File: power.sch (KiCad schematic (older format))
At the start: 13 parts, among them J9 POWER, U7 LM1117-3.3, U8 LM1117-5.0

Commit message: work on schematic
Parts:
- removed C3: 10u, Capacitors_SMD:CP_Elec_6.3x4.5, symbol CP1
- removed C4, C5, C6, C7: 22u, symbol CP1
- removed C8, C9: 100n, symbol C
- removed U7: LM1117-3.3, TO_SOT_Packages_SMD:SOT-223, symbol LM1117-3.3
- removed U8: LM1117-5.0, symbol LM1117-5.0
- added C201, C206, C211: 100n, Capacitors_SMD:C_0603, symbol CP1
- added C202, C207, C212: 22u, Capacitors_SMD:CP_Elec_5x5.8, symbol CP1
- added C203, C208, C209, C210, C213: 100n, Capacitors_SMD:C_0603, symbol C
- added C205: 47u, Capacitors_SMD:CP_Elec_6.3x5.7, symbol CP1
- added D202: LM4040CIM3-10.0, TO_SOT_Packages_SMD:SOT-23, symbol D_Schottky_ALT
- added D203: LM4040AIM3-2.0, TO_SOT_Packages_SMD:SOT-23, symbol D_Schottky_ALT
- added L201, L202, L203: Bead, Resistors_SMD:R_0603, symbol Ferrite_Bead
- added R201, R202: 1k, Resistors_SMD:R_0603, symbol R
- added R203: 10k, Resistors_SMD:R_0603, symbol R
- added U201, U202: LM1117-3.3, TO_SOT_Packages_SMD:SOT-223-3Lead_TabPin2, symbol LM1117-3.3
- added U203: LM1117-5.0, TO_SOT_Packages_SMD:SOT-223-3Lead_TabPin2, symbol LM1117-5.0
- added U204: STMPS2151, TO_SOT_Packages_SMD:SOT-23-5, symbol STMPS2141
- 1N5819HW201: renamed from D4; value D -> D204
- C204: renamed from C2; value 10u -> 47u; footprint Capacitors_SMD:CP_Elec_6.3x4.5 -> Capacitors_SMD:CP_Elec_6.3x5.7; MFN (none) -> Panasonic; MFP (none) -> EEE-FK1V470P
- D201: renamed from D3; value D -> 1N5819HW
- renumbered J9 to J201
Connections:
- net +12V: now also L201.2, L202.2, L203.2
- net +3.3VA: now also C207.1, C208.1, R202.1, U202.2 (VO)
- net +3V3: now also C202.1, C203.1, U201.2 (VO)
- net +5V: now also C212.1, C213.1, U203.2 (VO), U204.5 (IN)
- net -12V: now also C205.2, R201.1
- net GND: now also C201.2, C202.2, C203.2, C205.1, C206.2, C207.2, C208.2, C209.2, C210.2, C211.2, C212.2, C213.2, D202.1 (K), D203.2 (A), R203.2, U201.1 (GND), U202.1 (GND), U203.1 (GND), U204.2 (GND)
- net at J201.1 (Pin_1), J201.2 (Pin_2): now also 1N5819HW201.1 (K); no longer D201.2 (A)
- net at J201.10 (Pin_10), J201.9 (Pin_9): now also D201.2 (A); no longer 1N5819HW201.1 (K)
- new net: C201.1, L201.1, U201.3 (VI)
- new net: C206.1, L202.1, U202.3 (VI)
- new net: C211.1, L203.1, U203.3 (VI)
- new net AREF_-10V: C209.1, D202.2 (A), R201.2
- new net AREF_2.048V: C210.1, D203.1 (K), R202.2
- new net USB_5V: U204.1 (OUT)
- new net USB_PWR_EN: R203.1, U204.4 (EN)
- new net USB_PWR_FAULT: U204.3 (~FAULT)

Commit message: work in progress
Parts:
- C201, C203, C206, C208, C209, C210, C211, C213: MFN (none) -> Murata; MFP (none) -> GRM188R71E104JA01J
- D201: MFN (none) -> Diodes Inc.; MFP (none) -> 1N5819HW-7-F
- D204: renamed from 1N5819HW201; value D204 -> 1N5819HW; MFN (none) -> Diodes Inc.; MFP (none) -> 1N5819HW-7-F
- R201, R202: MFN (none) -> Panasonic; MFP (none) -> ERJ-3EKF1001V
- R203: MFN (none) -> Panasonic; MFP (none) -> ERJ-3EKF1002V

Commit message: work in progress
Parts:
- removed C201, C206, C211: 100n, Capacitors_SMD:C_0603, symbol CP1
- added C201, C206, C211: 100n, Capacitors_SMD:C_0603, symbol C
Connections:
- net GND: now also C201.2, C206.2, C211.2
- net at L201.1, U201.3 (VI): now also C201.1
- net at L202.1, U202.3 (VI): now also C206.1
- net at L203.1, U203.3 (VI): now also C211.1
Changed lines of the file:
@@
 $EndDescr
 $Comp
-L +12V #PWR022
+L +12V #PWR023
 U 1 1 59ADCE23
 P 1400 2500
-F 0 "#PWR022" H 1400 2350 50  0001 C CNN
+F 0 "#PWR023" H 1400 2350 50  0001 C CNN
 F 1 "+12V" H 1400 2640 50  0000 C CNN
 F 2 "" H 1400 2500 50  0001 C CNN
@@
 $EndComp
 $Comp
-L GND #PWR023
+L GND #PWR024
 U 1 1 59ADD2AE
 P 2800 2900
-F 0 "#PWR023" H 2800 2650 50  0001 C CNN
+F 0 "#PWR024" H 2800 2650 50  0001 C CNN
 F 1 "GND" H 2800 2750 50  0000 C CNN
 F 2 "" H 2800 2900 50  0001 C CNN
@@
 $EndComp
 $Comp
-L +12V #PWR024
+L +12V #PWR025
 U 1 1 59ADD597
 P 3800 2300
-F 0 "#PWR024" H 3800 2150 50  0001 C CNN
+F 0 "#PWR025" H 3800 2150 50  0001 C CNN
 F 1 "+12V" H 3800 2440 50  0000 C CNN
 F 2 "" H 3800 2300 50  0001 C CNN
@@
 $EndComp
 $Comp
-L GND #PWR025
+L GND #PWR026
 U 1 1 59ADD670
 P 3600 2900
-F 0 "#PWR025" H 3600 2650 50  0001 C CNN
+F 0 "#PWR026" H 3600 2650 50  0001 C CNN
 F 1 "GND" H 3600 2750 50  0000 C CNN
 F 2 "" H 3600 2900 50  0001 C CNN
@@
 $EndComp
 $Comp
-L CP1 C201
-U 1 1 59DEC568
-P 5300 1950
-F 0 "C201" H 5325 2050 50  0000 L CNN
-F 1 "100n" H 5325 1850 50  0000 L CNN
-F 2 "Capacitors_SMD:C_0603" H 5300 1950 50  0001 C CNN
-F 3 "http://datasheet.octopart.com/GRM188R71E104JA01J-Murata-datasheet-66077098.pdf" H 5300 1950 50  0001 C CNN
-F 4 "Murata" H 5325 2150 50  0001 C CNN "MFN"
-F 5 "GRM188R71E104JA01J" H 5325 2150 50  0001 C CNN "MFP"
-	1    5300 1950
-	1    0    0    -1
-$EndComp
-$Comp
 L CP1 C202
 U 1 1 59DEC56E
@@
 $EndComp
 $Comp
-L GND #PWR026
+L GND #PWR027
 U 1 1 59DEC57A
 P 5300 2200
-F 0 "#PWR026" H 5300 1950 50  0001 C CNN
+F 0 "#PWR027" H 5300 1950 50  0001 C CNN
 F 1 "GND" H 5300 2050 50  0000 C CNN
 F 2 "" H 5300 2200 50  0001 C CNN
@@
 $EndComp
 $Comp
-L GND #PWR027
+L GND #PWR028
 U 1 1 59DEC580
 P 6300 2200
-F 0 "#PWR027" H 6300 1950 50  0001 C CNN
+F 0 "#PWR028" H 6300 1950 50  0001 C CNN
 F 1 "GND" H 6300 2050 50  0000 C CNN
 F 2 "" H 6300 2200 50  0001 C CNN
@@
 $EndComp
 $Comp
-L GND #PWR028
+L GND #PWR029
 U 1 1 59DEC586
 P 6600 2200
-F 0 "#PWR028" H 6600 1950 50  0001 C CNN
+F 0 "#PWR029" H 6600 1950 50  0001 C CNN
 F 1 "GND" H 6600 2050 50  0000 C CNN
 F 2 "" H 6600 2200 50  0001 C CNN
@@
 $EndComp
 $Comp
-L +3V3 #PWR029
+L +3V3 #PWR030
 U 1 1 59DEC592
 P 6600 1600
-F 0 "#PWR029" H 6600 1450 50  0001 C CNN
+F 0 "#PWR030" H 6600 1450 50  0001 C CNN
 F 1 "+3V3" H 6600 1740 50  0000 C CNN
 F 2 "" H 6600 1600 50  0001 C CNN
@@
 $EndComp
 $Comp
-L GND #PWR030
+L GND #PWR031
 U 1 1 59DEC598
 P 5800 2200
-F 0 "#PWR030" H 5800 1950 50  0001 C CNN
+F 0 "#PWR031" H 5800 1950 50  0001 C CNN
 F 1 "GND" H 5800 2050 50  0000 C CNN
 F 2 "" H 5800 2200 50  0001 C CNN
@@
 $EndComp
 $Comp
-L CP1 C206
-U 1 1 59DEC800
-P 5300 3050
-F 0 "C206" H 5325 3150 50  0000 L CNN
-F 1 "100n" H 5325 2950 50  0000 L CNN
-F 2 "Capacitors_SMD:C_0603" H 5300 3050 50  0001 C CNN
-F 3 "http://datasheet.octopart.com/GRM188R71E104JA01J-Murata-datasheet-66077098.pdf" H 5300 3050 50  0001 C CNN
-F 4 "Murata" H 5325 3250 50  0001 C CNN "MFN"
-F 5 "GRM188R71E104JA01J" H 5325 3250 50  0001 C CNN "MFP"
-	1    5300 3050
-	1    0    0    -1
-$EndComp
-$Comp
 L C C208
 U 1 1 59DEC80C
@@
 $EndComp
 $Comp
-L GND #PWR031
+L GND #PWR032
 U 1 1 59DEC812
 P 5300 3300
-F 0 "#PWR031" H 5300 3050 50  0001 C CNN
+F 0 "#PWR032" H 5300 3050 50  0001 C CNN
 F 1 "GND" H 5300 3150 50  0000 C CNN
 F 2 "" H 5300 3300 50  0001 C CNN
@@
 $EndComp
 $Comp
-L GND #PWR032
+L GND #PWR033
 U 1 1 59DEC818
 P 6300 3300
-F 0 "#PWR032" H 6300 3050 50  0001 C CNN
+F 0 "#PWR033" H 6300 3050 50  0001 C CNN
 F 1 "GND" H 6300 3150 50  0000 C CNN
 F 2 "" H 6300 3300 50  0001 C CNN
@@
 $EndComp
 $Comp
-L GND #PWR033
+L GND #PWR034
 U 1 1 59DEC81E
 P 6600 3300
-F 0 "#PWR033" H 6600 3050 50  0001 C CNN
+F 0 "#PWR034" H 6600 3050 50  0001 C CNN
 F 1 "GND" H 6600 3150 50  0000 C CNN
 F 2 "" H 6600 3300 50  0001 C CNN
@@
 $EndComp
 $Comp
-L GND #PWR034
+L GND #PWR035
 U 1 1 59DEC82A
 P 5800 3300
-F 0 "#PWR034" H 5800 3050 50  0001 C CNN
+F 0 "#PWR035" H 5800 3050 50  0001 C CNN
 F 1 "GND" H 5800 3150 50  0000 C CNN
 F 2 "" H 5800 3300 50  0001 C CNN
@@
 $EndComp
 $Comp
-L +12V #PWR035
+L +12V #PWR036
 U 1 1 59DECCAB
 P 4800 1600
-F 0 "#PWR035" H 4800 1450 50  0001 C CNN
+F 0 "#PWR036" H 4800 1450 50  0001 C CNN
 F 1 "+12V" H 4800 1740 50  0000 C CNN
 F 2 "" H 4800 1600 50  0001 C CNN
@@
 $EndComp
 $Comp
-L +3.3VA #PWR036
+L +3.3VA #PWR037
 U 1 1 59DED3E1
 P 6600 2700
-F 0 "#PWR036" H 6600 2550 50  0001 C CNN
+F 0 "#PWR037" H 6600 2550 50  0001 C CNN
 F 1 "+3.3VA" H 6600 2840 50  0000 C CNN
 F 2 "" H 6600 2700 50  0001 C CNN
@@
 $EndComp
 $Comp
-L CP1 C211
-U 1 1 59DED9B9
-P 5300 4150
-F 0 "C211" H 5325 4250 50  0000 L CNN
-F 1 "100n" H 5325 4050 50  0000 L CNN
-F 2 "Capacitors_SMD:C_0603" H 5300 4150 50  0001 C CNN
-F 3 "http://datasheet.octopart.com/GRM188R71E104JA01J-Murata-datasheet-66077098.pdf" H 5300 4150 50  0001 C CNN
-F 4 "Murata" H 5325 4350 50  0001 C CNN "MFN"
-F 5 "GRM188R71E104JA01J" H 5325 4350 50  0001 C CNN "MFP"
-	1    5300 4150
-	1    0    0    -1
-$EndComp
-$Comp
 L C C213
 U 1 1 59DED9C5
@@
 $EndComp
 $Comp
-L GND #PWR037
+L GND #PWR038
 U 1 1 59DED9CB
 P 5300 4400
-F 0 "#PWR037" H 5300 4150 50  0001 C CNN
+F 0 "#PWR038" H 5300 4150 50  0001 C CNN
 F 1 "GND" H 5300 4250 50  0000 C CNN
 F 2 "" H 5300 4400 50  0001 C CNN
@@
 $EndComp
 $Comp
-L GND #PWR038
+L GND #PWR039
 U 1 1 59DED9D1
 P 6300 4400
-F 0 "#PWR038" H 6300 4150 50  0001 C CNN
+F 0 "#PWR039" H 6300 4150 50  0001 C CNN
 F 1 "GND" H 6300 4250 50  0000 C CNN
 F 2 "" H 6300 4400 50  0001 C CNN
@@
 $EndComp
 $Comp
-L GND #PWR039
+L GND #PWR040
 U 1 1 59DED9D7
 P 6600 4400
-F 0 "#PWR039" H 6600 4150 50  0001 C CNN
+F 0 "#PWR040" H 6600 4150 50  0001 C CNN
 F 1 "GND" H 6600 4250 50  0000 C CNN
 F 2 "" H 6600 4400 50  0001 C CNN
@@
 $EndComp
 $Comp
-L GND #PWR040
+L GND #PWR041
 U 1 1 59DED9DD
 P 5800 4400
-F 0 "#PWR040" H 5800 4150 50  0001 C CNN
+F 0 "#PWR041" H 5800 4150 50  0001 C CNN
 F 1 "GND" H 5800 4250 50  0000 C CNN
 F 2 "" H 5800 4400 50  0001 C CNN
@@
 $EndComp
 $Comp
-L +5V #PWR041
+L +5V #PWR042
 U 1 1 59DEDB3A
 P 6600 3800
-F 0 "#PWR041" H 6600 3650 50  0001 C CNN
+F 0 "#PWR042" H 6600 3650 50  0001 C CNN
 F 1 "+5V" H 6600 3940 50  0000 C CNN
 F 2 "" H 6600 3800 50  0001 C CNN
@@
 $EndComp
 $Comp
-L GND #PWR042
+L GND #PWR043
 U 1 1 59DF1FC9
 P 7900 3400
-F 0 "#PWR042" H 7900 3150 50  0001 C CNN
+F 0 "#PWR043" H 7900 3150 50  0001 C CNN
 F 1 "GND" H 7900 3250 50  0000 C CNN
 F 2 "" H 7900 3400 50  0001 C CNN
@@
 $EndComp
 $Comp
-L +5V #PWR043
+L +5V #PWR044
 U 1 1 59DFDC6E
 P 8400 4000
-F 0 "#PWR043" H 8400 3850 50  0001 C CNN
+F 0 "#PWR044" H 8400 3850 50  0001 C CNN
 F 1 "+5V" H 8400 4140 50  0000 C CNN
 F 2 "" H 8400 4000 50  0001 C CNN
@@
 $EndComp
 $Comp
-L GND #PWR044
+L GND #PWR045
 U 1 1 59DFDCE5
 P 8400 4700
-F 0 "#PWR044" H 8400 4450 50  0001 C CNN
+F 0 "#PWR045" H 8400 4450 50  0001 C CNN
 F 1 "GND" H 8400 4550 50  0000 C CNN
 F 2 "" H 8400 4700 50  0001 C CNN
@@
 $EndComp
 $Comp
-L GND #PWR045
+L GND #PWR046
 U 1 1 59E00E5E
 P 8200 4700
-F 0 "#PWR045" H 8200 4450 50  0001 C CNN
+F 0 "#PWR046" H 8200 4450 50  0001 C CNN
 F 1 "GND" H 8200 4550 50  0000 C CNN
 F 2 "" H 8200 4700 50  0001 C CNN
@@
 $EndComp
 $Comp
-L GND #PWR046
+L GND #PWR047
 U 1 1 59E08D7D
 P 9400 3400
-F 0 "#PWR046" H 9400 3150 50  0001 C CNN
+F 0 "#PWR047" H 9400 3150 50  0001 C CNN
 F 1 "GND" H 9400 3250 50  0000 C CNN
 F 2 "" H 9400 3400 50  0001 C CNN
@@
 $EndComp
 $Comp
-L +3.3VA #PWR047
+L +3.3VA #PWR048
 U 1 1 59E0BF07
 P 9400 2300
-F 0 "#PWR047" H 9400 2150 50  0001 C CNN
+F 0 "#PWR048" H 9400 2150 50  0001 C CNN
 F 1 "+3.3VA" H 9400 2440 50  0000 C CNN
 F 2 "" H 9400 2300 50  0001 C CNN
@@
 Connection ~ 7900 2800
 Connection ~ 9400 2800
+$Comp
+L C C201
+U 1 1 59E52EDD
+P 5300 1950
+F 0 "C201" H 5325 2050 50  0000 L CNN
+F 1 "100n" H 5325 1850 50  0000 L CNN
+F 2 "Capacitors_SMD:C_0603" H 5338 1800 50  0001 C CNN
+F 3 "http://datasheet.octopart.com/GRM188R71E104JA01J-Murata-datasheet-66077098.pdf" H 5300 1950 50  0001 C CNN
+F 4 "Murata" H 5300 1950 60  0001 C CNN "MFN"
+F 5 "GRM188R71E104JA01J" H 5300 1950 60  0001 C CNN "MFP"
+	1    5300 1950
+	1    0    0    -1
+$EndComp
+$Comp
+L C C206
+U 1 1 59E53513
+P 5300 3050
+F 0 "C206" H 5325 3150 50  0000 L CNN
+F 1 "100n" H 5325 2950 50  0000 L CNN
+F 2 "Capacitors_SMD:C_0603" H 5338 2900 50  0001 C CNN
+F 3 "http://datasheet.octopart.com/GRM188R71E104JA01J-Murata-datasheet-66077098.pdf" H 5300 3050 50  0001 C CNN
+F 4 "Murata" H 5300 3050 60  0001 C CNN "MFN"
+F 5 "GRM188R71E104JA01J" H 5300 3050 60  0001 C CNN "MFP"
+	1    5300 3050
+	1    0    0    -1
+$EndComp
+$Comp
+L C C211
+U 1 1 59E535E8
+P 5300 4150
+F 0 "C211" H 5325 4250 50  0000 L CNN
+F 1 "100n" H 5325 4050 50  0000 L CNN
+F 2 "Capacitors_SMD:C_0603" H 5338 4000 50  0001 C CNN
+F 3 "http://datasheet.octopart.com/GRM188R71E104JA01J-Murata-datasheet-66077098.pdf" H 5300 4150 50  0001 C CNN
+F 4 "Murata" H 5300 4150 60  0001 C CNN "MFN"
+F 5 "GRM188R71E104JA01J" H 5300 4150 60  0001 C CNN "MFP"
+	1    5300 4150
+	1    0    0    -1
+$EndComp
 $EndSCHEMATC

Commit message: redesign in progress
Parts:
- removed C210: 100n, Capacitors_SMD:C_0603, symbol C
- removed D203: LM4040AIM3-2.0, TO_SOT_Packages_SMD:SOT-23, symbol D_Schottky_ALT
- removed R202: 1k, Resistors_SMD:R_0603, symbol R

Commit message: only ground plane left
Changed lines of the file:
@@
 $EndDescr
 $Comp
-L +12V #PWR210
+L +12V #PWR023
 U 1 1 59ADCE23
 P 1400 2500
-F 0 "#PWR210" H 1400 2350 50  0001 C CNN
+F 0 "#PWR023" H 1400 2350 50  0001 C CNN
 F 1 "+12V" H 1400 2640 50  0000 C CNN
 F 2 "" H 1400 2500 50  0001 C CNN
@@
 $EndComp
 $Comp
-L -12V #PWR214
+L -12V #PWR213
 U 1 1 59ADCE37
 P 1400 3100
-F 0 "#PWR214" H 1400 3200 50  0001 C CNN
+F 0 "#PWR213" H 1400 3200 50  0001 C CNN
 F 1 "-12V" H 1400 3250 50  0000 C CNN
 F 2 "" H 1400 3100 50  0001 C CNN
@@
 $EndComp
 $Comp
-L GND #PWR212
+L GND #PWR024
 U 1 1 59ADD2AE
 P 2800 2900
-F 0 "#PWR212" H 2800 2650 50  0001 C CNN
+F 0 "#PWR024" H 2800 2650 50  0001 C CNN
 F 1 "GND" H 2800 2750 50  0000 C CNN
 F 2 "" H 2800 2900 50  0001 C CNN
@@
 $EndComp
 $Comp
-L -12V #PWR215
+L -12V #PWR214
 U 1 1 59ADD571
 P 3800 3300
-F 0 "#PWR215" H 3800 3400 50  0001 C CNN
+F 0 "#PWR214" H 3800 3400 50  0001 C CNN
 F 1 "-12V" H 3800 3450 50  0000 C CNN
 F 2 "" H 3800 3300 50  0001 C CNN
@@
 $EndComp
 $Comp
-L +12V #PWR207
+L +12V #PWR025
 U 1 1 59ADD597
 P 3800 2300
-F 0 "#PWR207" H 3800 2150 50  0001 C CNN
+F 0 "#PWR025" H 3800 2150 50  0001 C CNN
 F 1 "+12V" H 3800 2440 50  0000 C CNN
 F 2 "" H 3800 2300 50  0001 C CNN
@@
 $EndComp
 $Comp
-L GND #PWR213
+L GND #PWR026
 U 1 1 59ADD670
 P 3600 2900
-F 0 "#PWR213" H 3600 2650 50  0001 C CNN
+F 0 "#PWR026" H 3600 2650 50  0001 C CNN
 F 1 "GND" H 3600 2750 50  0000 C CNN
 F 2 "" H 3600 2900 50  0001 C CNN
@@
 $EndComp
 $Comp
-L GND #PWR203
+L GND #PWR027
 U 1 1 59DEC57A
 P 5300 2200
-F 0 "#PWR203" H 5300 1950 50  0001 C CNN
+F 0 "#PWR027" H 5300 1950 50  0001 C CNN
 F 1 "GND" H 5300 2050 50  0000 C CNN
 F 2 "" H 5300 2200 50  0001 C CNN
@@
 $EndComp
 $Comp
-L GND #PWR205
+L GND #PWR028
 U 1 1 59DEC580
 P 6300 2200
-F 0 "#PWR205" H 6300 1950 50  0001 C CNN
+F 0 "#PWR028" H 6300 1950 50  0001 C CNN
 F 1 "GND" H 6300 2050 50  0000 C CNN
 F 2 "" H 6300 2200 50  0001 C CNN
@@
 $EndComp
 $Comp
-L GND #PWR206
+L GND #PWR029
 U 1 1 59DEC586
 P 6600 2200
-F 0 "#PWR206" H 6600 1950 50  0001 C CNN
+F 0 "#PWR029" H 6600 1950 50  0001 C CNN
 F 1 "GND" H 6600 2050 50  0000 C CNN
 F 2 "" H 6600 2200 50  0001 C CNN
@@
 $EndComp
 $Comp
-L +3V3 #PWR202
+L +3V3 #PWR030
 U 1 1 59DEC592
 P 6600 1600
-F 0 "#PWR202" H 6600 1450 50  0001 C CNN
+F 0 "#PWR030" H 6600 1450 50  0001 C CNN
 F 1 "+3V3" H 6600 1740 50  0000 C CNN
 F 2 "" H 6600 1600 50  0001 C CNN
@@
 $EndComp
 $Comp
-L GND #PWR204
+L GND #PWR031
 U 1 1 59DEC598
 P 5800 2200
-F 0 "#PWR204" H 5800 1950 50  0001 C CNN
+F 0 "#PWR031" H 5800 1950 50  0001 C CNN
 F 1 "GND" H 5800 2050 50  0000 C CNN
 F 2 "" H 5800 2200 50  0001 C CNN
@@
 $EndComp
 $Comp
-L GND #PWR216
+L GND #PWR032
 U 1 1 59DEC812
 P 5300 3300
-F 0 "#PWR216" H 5300 3050 50  0001 C CNN
+F 0 "#PWR032" H 5300 3050 50  0001 C CNN
 F 1 "GND" H 5300 3150 50  0000 C CNN
 F 2 "" H 5300 3300 50  0001 C CNN
@@
 $EndComp
 $Comp
-L GND #PWR218
+L GND #PWR033
 U 1 1 59DEC818
 P 6300 3300
-F 0 "#PWR218" H 6300 3050 50  0001 C CNN
+F 0 "#PWR033" H 6300 3050 50  0001 C CNN
 F 1 "GND" H 6300 3150 50  0000 C CNN
 F 2 "" H 6300 3300 50  0001 C CNN
@@
 $EndComp
 $Comp
-L GND #PWR219
+L GND #PWR034
 U 1 1 59DEC81E
 P 6600 3300
-F 0 "#PWR219" H 6600 3050 50  0001 C CNN
+F 0 "#PWR034" H 6600 3050 50  0001 C CNN
 F 1 "GND" H 6600 3150 50  0000 C CNN
 F 2 "" H 6600 3300 50  0001 C CNN
@@
 $EndComp
 $Comp
-L GND #PWR217
+L GND #PWR035
 U 1 1 59DEC82A
 P 5800 3300
-F 0 "#PWR217" H 5800 3050 50  0001 C CNN
+F 0 "#PWR035" H 5800 3050 50  0001 C CNN
 F 1 "GND" H 5800 3150 50  0000 C CNN
 F 2 "" H 5800 3300 50  0001 C CNN
@@
 $EndComp
 $Comp
-L +12V #PWR201
+L +12V #PWR036
 U 1 1 59DECCAB
 P 4800 1600
-F 0 "#PWR201" H 4800 1450 50  0001 C CNN
+F 0 "#PWR036" H 4800 1450 50  0001 C CNN
 F 1 "+12V" H 4800 1740 50  0000 C CNN
 F 2 "" H 4800 1600 50  0001 C CNN
@@
 $EndComp
 $Comp
-L +3.3VA #PWR211
+L +3.3VA #PWR037
 U 1 1 59DED3E1
 P 6600 2700
-F 0 "#PWR211" H 6600 2550 50  0001 C CNN
+F 0 "#PWR037" H 6600 2550 50  0001 C CNN
 F 1 "+3.3VA" H 6600 2840 50  0000 C CNN
 F 2 "" H 6600 2700 50  0001 C CNN
@@
 $EndComp
 $Comp
-L GND #PWR224
+L GND #PWR038
 U 1 1 59DED9CB
 P 5300 4400
-F 0 "#PWR224" H 5300 4150 50  0001 C CNN
+F 0 "#PWR038" H 5300 4150 50  0001 C CNN
 F 1 "GND" H 5300 4250 50  0000 C CNN
 F 2 "" H 5300 4400 50  0001 C CNN
@@
 $EndComp
 $Comp
-L GND #PWR226
+L GND #PWR039
 U 1 1 59DED9D1
 P 6300 4400
-F 0 "#PWR226" H 6300 4150 50  0001 C CNN
+F 0 "#PWR039" H 6300 4150 50  0001 C CNN
 F 1 "GND" H 6300 4250 50  0000 C CNN
 F 2 "" H 6300 4400 50  0001 C CNN
@@
 $EndComp
 $Comp
-L GND #PWR227
+L GND #PWR040
 U 1 1 59DED9D7
 P 6600 4400
-F 0 "#PWR227" H 6600 4150 50  0001 C CNN
+F 0 "#PWR040" H 6600 4150 50  0001 C CNN
 F 1 "GND" H 6600 4250 50  0000 C CNN
 F 2 "" H 6600 4400 50  0001 C CNN
@@
 $EndComp
 $Comp
-L GND #PWR225
+L GND #PWR041
 U 1 1 59DED9DD
 P 5800 4400
-F 0 "#PWR225" H 5800 4150 50  0001 C CNN
+F 0 "#PWR041" H 5800 4150 50  0001 C CNN
 F 1 "GND" H 5800 4250 50  0000 C CNN
 F 2 "" H 5800 4400 50  0001 C CNN
@@
 $EndComp
 $Comp
-L +5V #PWR222
+L +5V #PWR042
 U 1 1 59DEDB3A
 P 6600 3800
-F 0 "#PWR222" H 6600 3650 50  0001 C CNN
+F 0 "#PWR042" H 6600 3650 50  0001 C CNN
 F 1 "+5V" H 6600 3940 50  0000 C CNN
 F 2 "" H 6600 3800 50  0001 C CNN
@@
 $EndComp
 $Comp
-L GND #PWR220
+L GND #PWR043
 U 1 1 59DF1FC9
 P 7900 3400
-F 0 "#PWR220" H 7900 3150 50  0001 C CNN
+F 0 "#PWR043" H 7900 3150 50  0001 C CNN
 F 1 "GND" H 7900 3250 50  0000 C CNN
 F 2 "" H 7900 3400 50  0001 C CNN
@@
 $EndComp
 $Comp
-L +5V #PWR223
+L +5V #PWR044
 U 1 1 59DFDC6E
 P 8400 4000
-F 0 "#PWR223" H 8400 3850 50  0001 C CNN
+F 0 "#PWR044" H 8400 3850 50  0001 C CNN
 F 1 "+5V" H 8400 4140 50  0000 C CNN
 F 2 "" H 8400 4000 50  0001 C CNN
@@
 $EndComp
 $Comp
-L GND #PWR229
+L GND #PWR045
 U 1 1 59DFDCE5
 P 8400 4700
-F 0 "#PWR229" H 8400 4450 50  0001 C CNN
+F 0 "#PWR045" H 8400 4450 50  0001 C CNN
 F 1 "GND" H 8400 4550 50  0000 C CNN
 F 2 "" H 8400 4700 50  0001 C CNN
@@
 $EndComp
 $Comp
-L GND #PWR228
+L GND #PWR046
 U 1 1 59E00E5E
 P 8200 4700
-F 0 "#PWR228" H 8200 4450 50  0001 C CNN
+F 0 "#PWR046" H 8200 4450 50  0001 C CNN
 F 1 "GND" H 8200 4550 50  0000 C CNN
 F 2 "" H 8200 4700 50  0001 C CNN
@@
 	1400 3000 1400 3100
 Wire Wire Line
-	1800 2600 2500 2600
-Wire Wire Line
-	1800 3000 2500 3000
-Wire Wire Line
 	2000 2700 2600 2700
 Wire Wire Line
@@
 	5800 2000 5800 2200
 Wire Wire Line
-	5300 1700 5300 1800
+	5300 1600 5300 1800
 Wire Wire Line
 	5200 2800 5500 2800
@@
 	5800 3100 5800 3300
 Wire Wire Line
-	5300 2800 5300 2900
+	5300 2700 5300 2900
 Wire Wire Line
 	4800 2800 4900 2800
@@
 	4800 1600 4800 3900
 Wire Wire Line
-	4800 1700 4900 1700
-Wire Wire Line
 	5200 3900 5500 3900
 Wire Wire Line
@@
 	5800 4200 5800 4400
 Wire Wire Line
-	5300 3900 5300 4000
+	5300 3800 5300 4000
 Wire Wire Line
 	4800 3900 4900 3900
@@
 Connection ~ 8200 4200
 Connection ~ 7900 2800
+Wire Wire Line
+	4800 1700 4900 1700
+Wire Wire Line
+	1800 2600 2500 2600
+Wire Wire Line
+	1800 3000 2500 3000
+$Comp
+L PWR_FLAG #FLG047
+U 1 1 59F34CFD
+P 5300 1600
+F 0 "#FLG047" H 5300 1675 50  0001 C CNN
+F 1 "PWR_FLAG" H 5300 1750 50  0000 C CNN
+F 2 "" H 5300 1600 50  0001 C CNN
+F 3 "" H 5300 1600 50  0001 C CNN
+	1    5300 1600
+	1    0    0    -1
+$EndComp
+$Comp
+L PWR_FLAG #FLG048
+U 1 1 59F34D75
+P 5300 2700
+F 0 "#FLG048" H 5300 2775 50  0001 C CNN
+F 1 "PWR_FLAG" H 5300 2850 50  0000 C CNN
+F 2 "" H 5300 2700 50  0001 C CNN
+F 3 "" H 5300 2700 50  0001 C CNN
+	1    5300 2700
+	1    0    0    -1
+$EndComp
+$Comp
+L PWR_FLAG #FLG049
+U 1 1 59F34F89
+P 5300 3800
+F 0 "#FLG049" H 5300 3875 50  0001 C CNN
+F 1 "PWR_FLAG" H 5300 3950 50  0000 C CNN
+F 2 "" H 5300 3800 50  0001 C CNN
+F 3 "" H 5300 3800 50  0001 C CNN
+	1    5300 3800
+	1    0    0    -1
+$EndComp
 $EndSCHEMATC

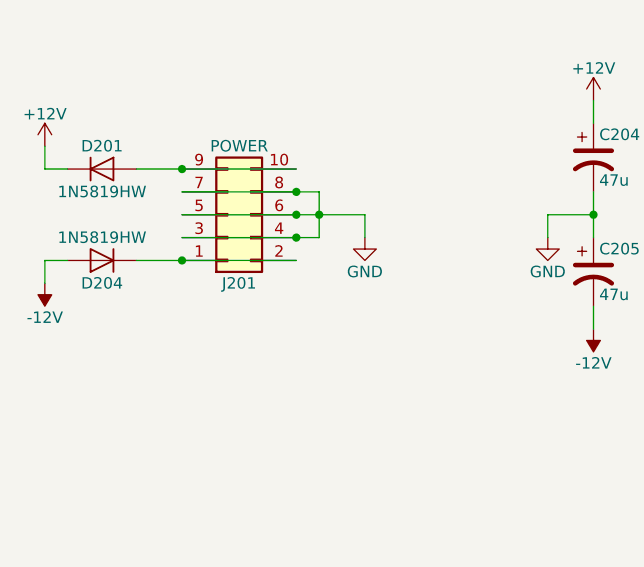
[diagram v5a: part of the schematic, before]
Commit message: renamed header references to JPxxx
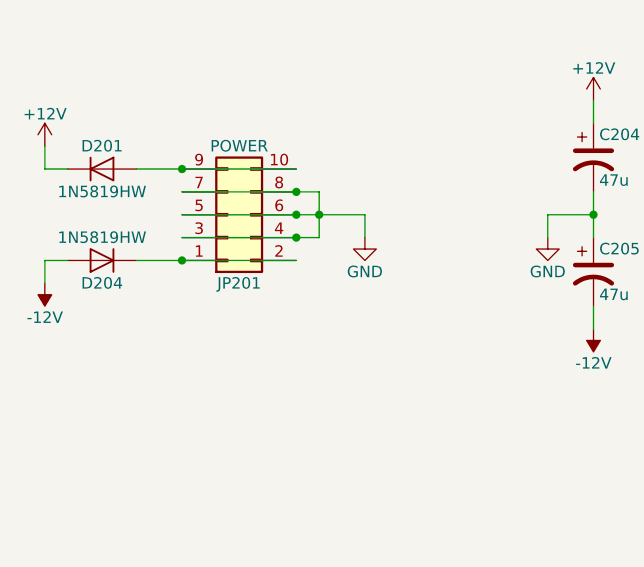
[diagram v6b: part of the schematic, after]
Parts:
- renumbered J201 to JP201
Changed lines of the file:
@@
 $EndComp
 $Comp
-L Conn_02x05_Odd_Even J201
+L Conn_02x05_Odd_Even JP201
 U 1 1 59ADD000
 P 2200 2800
-F 0 "J201" H 2250 3100 50  0000 C CNN
+F 0 "JP201" H 2250 3100 50  0000 C CNN
 F 1 "POWER" H 2250 2500 50  0000 C CNN
 F 2 "Pin_Headers:Pin_Header_Straight_2x05_Pitch2.54mm" H 2200 2800 50  0001 C CNN

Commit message: work in progress
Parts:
- C201, C203, C206, C208, C209, C211, C213: footprint Capacitors_SMD:C_0603 -> Capacitors_SMD:C_0603_HandSoldering
- L201, L202, L203, R201, R203: footprint Resistors_SMD:R_0603 -> Resistors_SMD:R_0603_HandSoldering
